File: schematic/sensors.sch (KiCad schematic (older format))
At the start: 33 parts, among them J10 Conn_01x03, J11 Conn_01x03, J15 Conn_01x03_Female, J6 Conn_01x03, J7 Conn_01x02, J8 Conn_01x03_Female, J9 Conn_01x03, U10 MAX6682MUA+T, U3 ADS1015IDGS, U4 FAN4860UC5X, U5 LIS2MDL, U6 LSM6DSOX, U7 BME280, U9 MC74HC138A

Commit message: wireing
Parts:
- U10: symbol eec:MAX6682MUA+T -> Apsu-rescue:MAX6682MUA+T-eec
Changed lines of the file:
@@
 Connection ~ 3950 3200
 $Comp
-L eec:MAX6682MUA+T U10
+L Apsu-rescue:MAX6682MUA+T-eec U10
 U 1 1 5EFF1BCA
 P 6550 4200
+AR Path="/5EFF1BCA" Ref="U10"  Part="1"
+AR Path="/5EF89400/5EFF1BCA" Ref="U10"  Part="1"
 F 0 "U10" H 6950 4465 50  0000 C CNN
 F 1 "MAX6682MUA+T" H 6950 4374 50  0000 C CNN

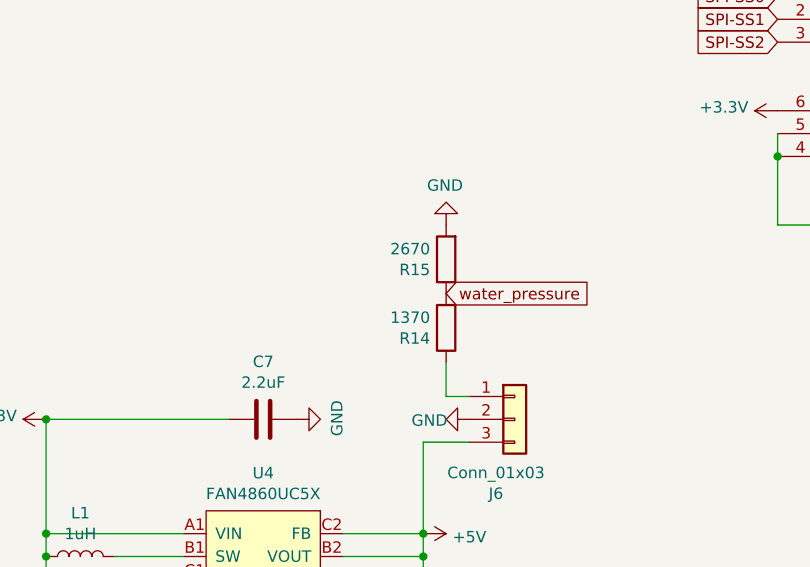
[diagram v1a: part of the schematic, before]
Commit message: added MPN
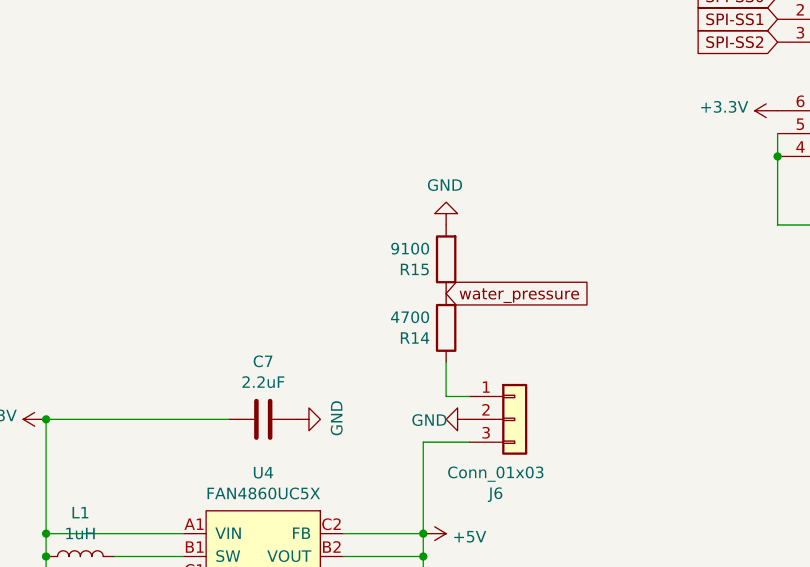
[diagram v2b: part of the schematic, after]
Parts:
- C10, C11, C13, C14, C15, C16, C19, C20, C21, C5, C6: MPN (none) -> C0805C104J5RACTU
- C12: MPN (none) -> C0805C106K8PACTU
- C7: MPN (none) -> C0805C225K4RACTU
- C8: MPN (none) -> C0805C475K3PACTU
- C9: MPN (none) -> C0805C224K5RACTU
- L1: MPN (none) -> LQM21NN1R0K10D
- R14: value 1370 -> 4700; MPN (none) -> ERA-6AEB472V
- R15: value 2670 -> 9100
- R26: MPN (none) -> ERA-6AEB301V
- U10: MPN (none) -> MAX6682MUA+T
- U3: MPN (none) -> ADS1015IDGS
- U4: MPN (none) -> FAN4860UC5X
- U5: MPN (none) -> LIS2MDLTR
- U6: MPN (none) -> LSM6DSOXTR
- U7: MPN (none) -> BME280
- U9: MPN (none) -> MC74HC138ADTR2G

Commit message: added MPN for connectors
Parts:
- J10, J11, J15, J6, J8, J9: MPN (none) -> B3B-XH-A(LF)(SN)
- J7: MPN (none) -> B2B-XH-A(LF)(SN)
- R15: MPN (none) -> ERA6AEB912V
